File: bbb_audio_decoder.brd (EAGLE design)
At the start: 113 x 100 mm, 186 parts, among them IC1 OPA2134, IC2 LM317, IC3 LM337, IC4 OPA2134, IC5 OPA2134, IC6 OPA2134, IC7 LM317, P1 PLR135/T9, Q2 BS170, U1 PCM1690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

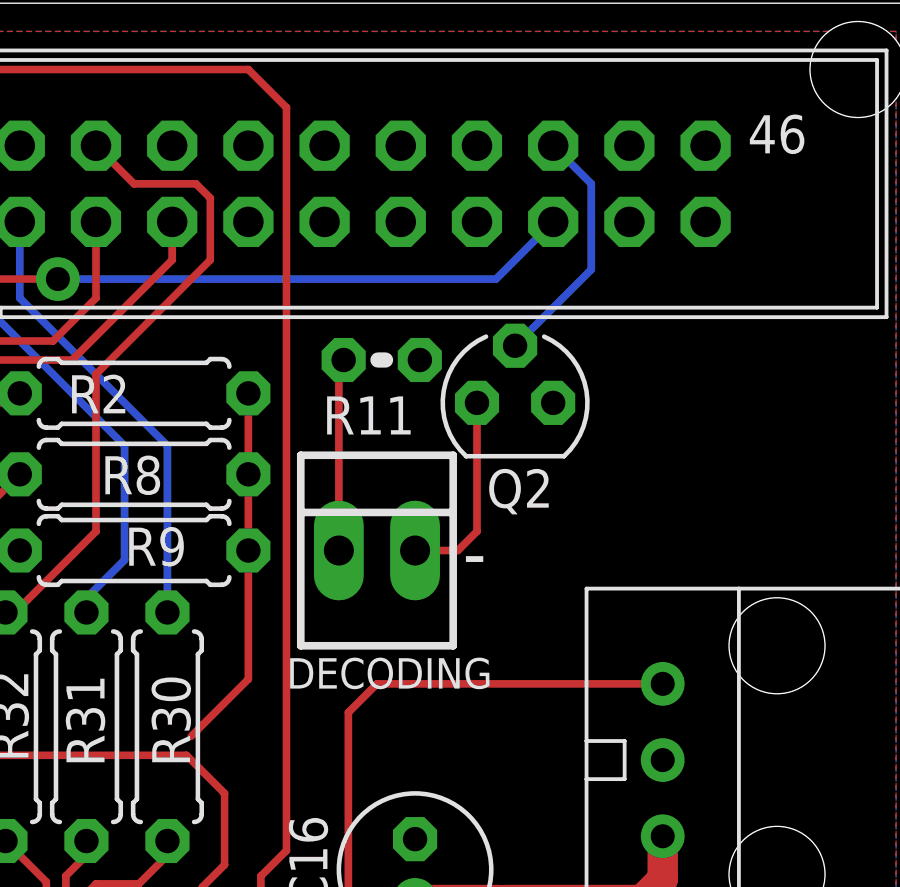
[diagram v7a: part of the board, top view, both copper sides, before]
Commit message: Replaced LED with 1206 SMD one
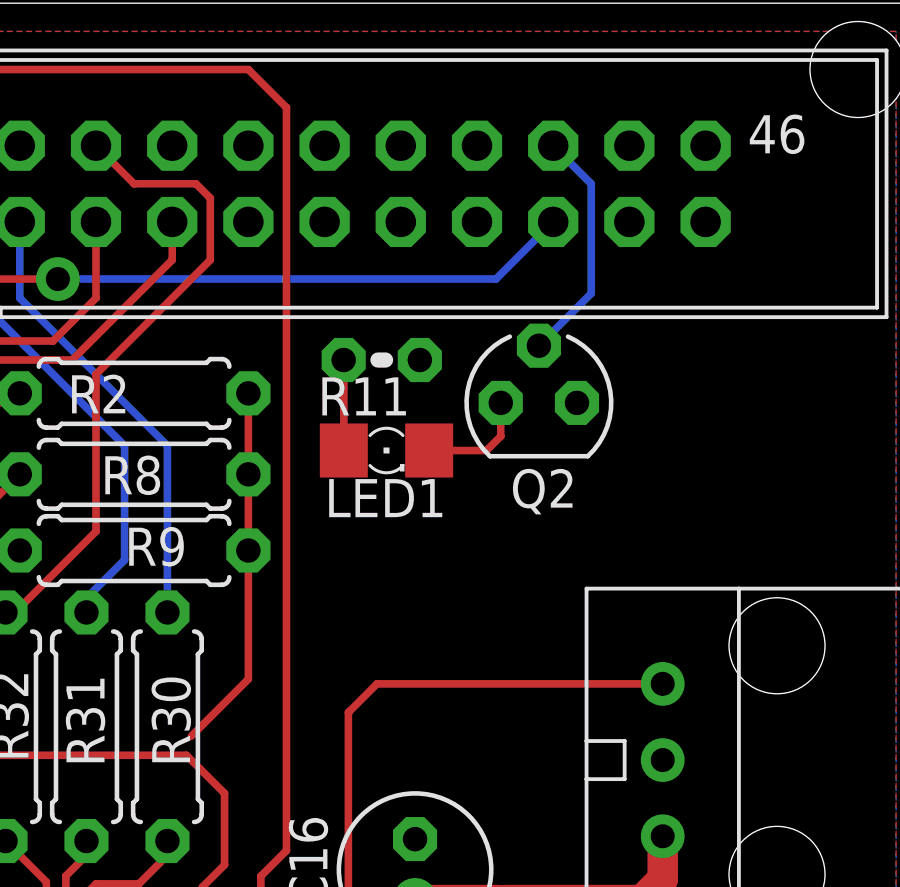
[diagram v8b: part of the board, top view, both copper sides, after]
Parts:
- removed DECODING: 22-23-2021, con-molex:22-23-2021
- added LED1: (no value), led:1206
- moved Q2 0.79 mm to (99.9, 86.7)
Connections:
- removed net N$91: DECODING.2, Q2.D
- removed net N$92: DECODING.1, R11.1
- new net N$28: LED1.C, Q2.D
- new net N$4: LED1.A, R11.1
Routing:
- net N$91: track 6.61 -> 0.00 mm
- net N$92: track 6.42 -> 0.00 mm
- net N$28: track 0.00 -> 3.70 mm
- net N$4: track 0.00 -> 3.02 mm
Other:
- board text removed: "-"
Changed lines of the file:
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@@
 <hole x="110.49" y="2.54" drill="3.2"/>
 <hole x="3.81" y="2.54" drill="3.2"/>
-<text x="97.31375" y="80.80375" size="1.778" layer="21">-</text>
 <text x="84.93125" y="2.8575" size="1.016" layer="21">GND</text>
 <text x="60.6425" y="2.54" size="1.016" layer="21">GND</text>
@@
 <attribute name="VALUE" x="44.8564" y="73.8886" size="1.27" layer="27" ratio="10"/>
 </element>
-<element name="Q2" library="transistor-small-signal" package="SOT54E" value="BS170" x="99.06" y="86.6775" smashed="yes">
-<attribute name="VALUE" x="102.235" y="84.7725" size="1.27" layer="27" ratio="10"/>
-<attribute name="NAME" x="98.1075" y="83.185" size="1.27" layer="25" ratio="10"/>
+<element name="Q2" library="transistor-small-signal" package="SOT54E" value="BS170" x="99.85375" y="86.6775" smashed="yes">
+<attribute name="VALUE" x="103.02875" y="84.7725" size="1.27" layer="27" ratio="10"/>
+<attribute name="NAME" x="98.90125" y="83.185" size="1.27" layer="25" ratio="10"/>
 </element>
 <element name="R11" library="rcl" package="0204V" value="120" x="94.615" y="88.10625" smashed="yes">
-<attribute name="NAME" x="92.64015" y="85.6234" size="1.27" layer="25" ratio="10"/>
+<attribute name="NAME" x="92.4814" y="86.2584" size="1.27" layer="25" ratio="10"/>
 <attribute name="VALUE" x="92.4814" y="85.79485" size="1.27" layer="27" ratio="10"/>
-</element>
-<element name="DECODING" library="con-molex" package="22-23-2021" value="22-23-2021" x="94.45625" y="81.75625" smashed="yes">
-<attribute name="MPN" value="22-23-2021" x="94.45625" y="81.75625" size="1.778" layer="27" display="off"/>
-<attribute name="OC_NEWARK" value="25C3832" x="94.45625" y="81.75625" size="1.778" layer="27" display="off"/>
-<attribute name="MF" value="MOLEX" x="94.45625" y="81.75625" size="1.778" layer="27" display="off"/>
-<attribute name="OC_FARNELL" value="1462926" x="94.45625" y="81.75625" size="1.778" layer="27" display="off"/>
-<attribute name="NAME" x="91.44" y="77.1525" size="1.016" layer="25" ratio="10"/>
-<attribute name="VALUE" x="91.91625" y="76.67625" size="1.016" layer="27" ratio="10"/>
 </element>
 <element name="OUT1" library="con-molex" package="22-23-2021" value="22-23-2021" x="96.36125" y="3.175" smashed="yes">
@@
 <attribute name="NAME" x="49.08065" y="81.3801" size="1.016" layer="25" ratio="10"/>
 <attribute name="VALUE" x="49.08065" y="81.1261" size="0.8128" layer="27" ratio="10"/>
+</element>
+<element name="LED1" library="led" package="1206" value="" x="94.77375" y="85.09" smashed="yes">
+<attribute name="NAME" x="92.71" y="82.8675" size="1.27" layer="25"/>
+<attribute name="VALUE" x="93.50375" y="82.55" size="1.27" layer="27"/>
 </element>
 </elements>
@@
 <wire x1="103.98125" y1="70.8025" x2="103.98125" y2="72.23125" width="1.016" layer="1"/>
 </signal>
-<signal name="N$91">
-<contactref element="Q2" pad="D"/>
-<contactref element="DECODING" pad="2"/>
-<wire x1="95.72625" y1="81.75625" x2="97.155" y2="81.75625" width="0.254" layer="1"/>
-<wire x1="97.155" y1="81.75625" x2="97.79" y2="82.39125" width="0.254" layer="1"/>
-<wire x1="97.79" y1="82.39125" x2="97.79" y2="86.6775" width="0.254" layer="1"/>
-</signal>
-<signal name="N$92">
-<contactref element="R11" pad="1"/>
-<contactref element="DECODING" pad="1"/>
-<wire x1="93.18625" y1="81.75625" x2="93.18625" y2="87.9475" width="0.254" layer="1"/>
-<wire x1="93.18625" y1="87.9475" x2="93.345" y2="88.10625" width="0.254" layer="1"/>
-</signal>
 <signal name="N$94">
 <contactref element="Q2" pad="G"/>
 <contactref element="U$1" pad="42"/>
 <wire x1="100.33" y1="95.25" x2="101.6" y2="93.98" width="0.254" layer="16"/>
-<wire x1="101.6" y1="93.98" x2="101.6" y2="91.1225" width="0.254" layer="16"/>
-<wire x1="101.6" y1="91.1225" x2="99.06" y2="88.5825" width="0.254" layer="16"/>
+<wire x1="101.6" y1="93.98" x2="101.6" y2="90.32875" width="0.254" layer="16"/>
+<wire x1="101.6" y1="90.32875" x2="99.85375" y2="88.5825" width="0.254" layer="16"/>
 </signal>
 <signal name="N$37">
@@
 <wire x1="5.61405" y1="84.9884" x2="10.63625" y2="79.9662" width="0.8128" layer="1"/>
 </signal>
+<signal name="N$4">
+<contactref element="R11" pad="1"/>
+<contactref element="LED1" pad="A"/>
+<wire x1="93.35175" y1="85.09" x2="93.35175" y2="88.0995" width="0.254" layer="1"/>
+<wire x1="93.35175" y1="88.0995" x2="93.345" y2="88.10625" width="0.254" layer="1"/>
+</signal>
+<signal name="N$28">
+<contactref element="LED1" pad="C"/>
+<contactref element="Q2" pad="D"/>
+<wire x1="96.19575" y1="85.09" x2="98.1075" y2="85.09" width="0.254" layer="1"/>
+<wire x1="98.1075" y1="85.09" x2="98.58375" y2="85.56625" width="0.254" layer="1"/>
+<wire x1="98.58375" y1="85.56625" x2="98.58375" y2="86.6775" width="0.254" layer="1"/>
+</signal>
 </signals>
